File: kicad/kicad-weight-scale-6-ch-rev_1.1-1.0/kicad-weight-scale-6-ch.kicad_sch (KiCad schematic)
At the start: 29 parts, among them J1 9VDC, J2 Reset, J3 Serial, J4 Serial1, J5 Serial2, J6 Conn_01x02, J7 Conn_01x02, J8 Conn_01x02, P1 CH1, P2 CH1, P3 CH1, P4 CH1, P5 CH1, P6 CH1, U1 LM2596S-5, U2 WCMCU-ADS1232, U3 ESPWROOM32, U4 WCMCU-ADS1232, U5 DataLoggingBoard, U6 WCMCU-ADS1232

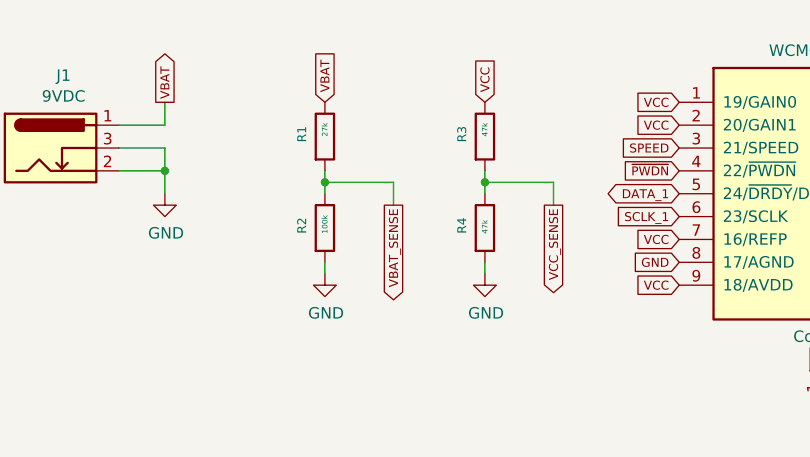
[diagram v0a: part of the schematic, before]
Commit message: Update PCB file and place an order to JLCPCB
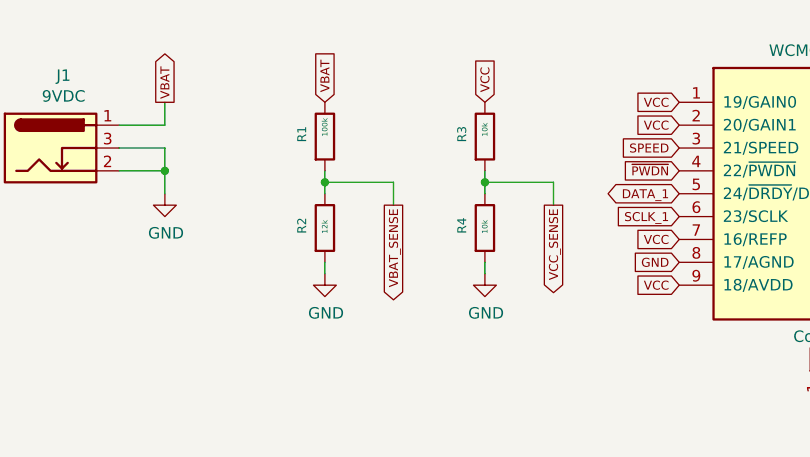
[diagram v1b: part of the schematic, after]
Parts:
- R1: value 27k -> 100k
- R2: value 100k -> 12k
- R3, R4: value 47k -> 10k
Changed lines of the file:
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@@
 			)
 		)
-		(property "Value" "27k"
+		(property "Value" "100k"
 			(at 76.2 29.21 90)
 			(effects
@@
 			)
 		)
-		(property "Value" "100k"
+		(property "Value" "12k"
 			(at 76.2 40.005 90)
 			(effects
@@
 			)
 		)
-		(property "Value" "47k"
+		(property "Value" "10k"
 			(at 93.98 40.005 90)
 			(effects
@@
 			)
 		)
-		(property "Value" "47k"
+		(property "Value" "10k"
 			(at 93.98 29.21 90)
 			(effects
